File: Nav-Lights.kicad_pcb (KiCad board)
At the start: 4 copper layers, 40 x 10 mm, 29 parts, among them J1 Conn_01x02_Pin, U1 LMC555CMMX, U2 TPS7B8133QWDRVRQ1, U3 LT8374RUFM-WPBF

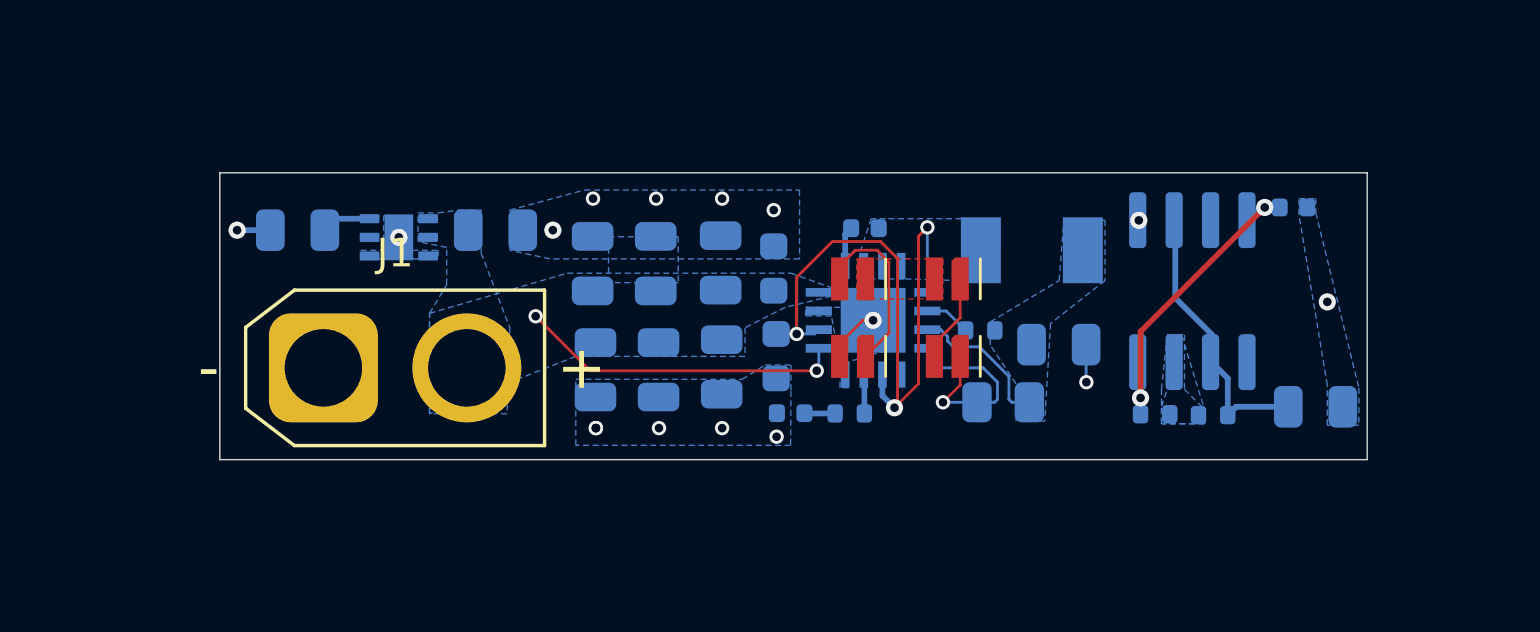
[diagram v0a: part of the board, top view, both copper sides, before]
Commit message: Adding in voltage divider for signal and layout and prod files
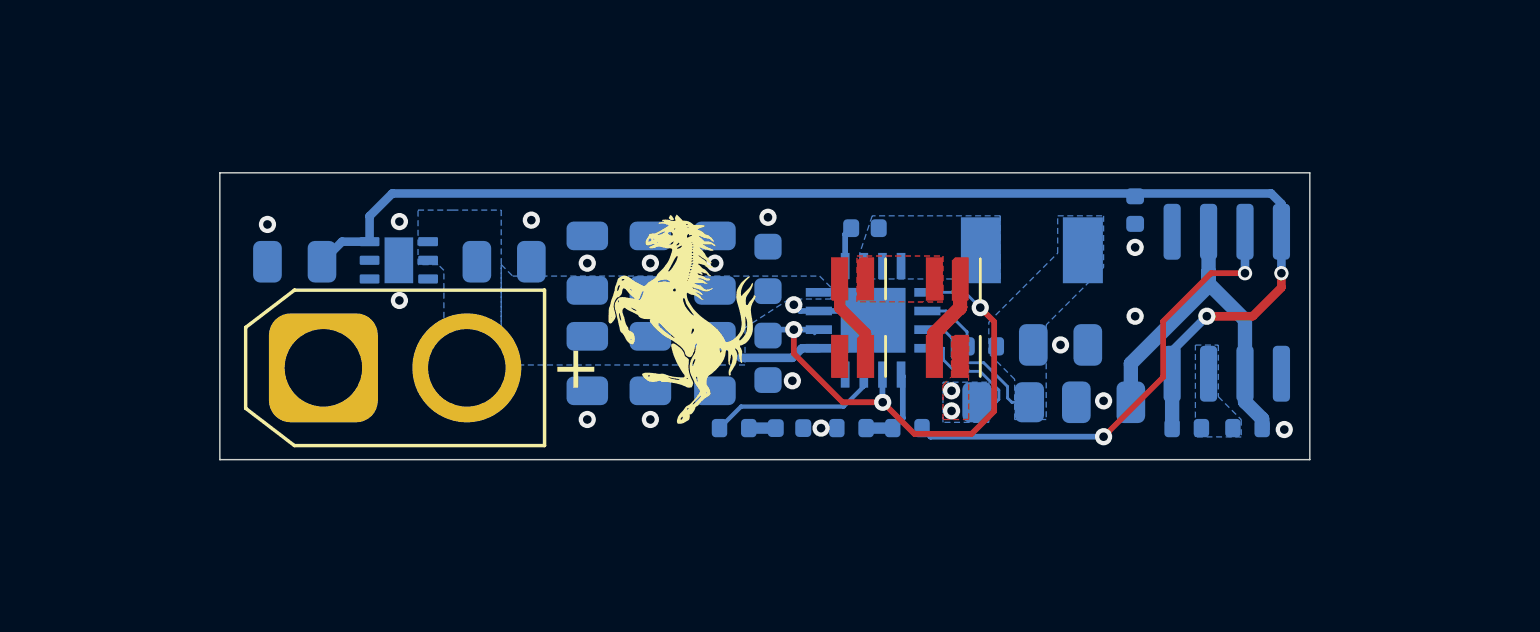
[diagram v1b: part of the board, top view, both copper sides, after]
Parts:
- added G***1: LOGO, LOGO, F.Cu at (143.4, 94.5)
- added R6: R_US, Resistor_SMD:R_0402_1005Metric, B.Cu at (151.3, 98.3)
- added R7: R_US, Resistor_SMD:R_0402_1005Metric, B.Cu at (149.3, 98.3)
- moved C3 7.39 mm to (158.1, 97.4), turned to 180 degrees
- moved C4 5.52 mm to (159.2, 90.7), turned to -90 degrees
- moved R4 4.06 mm to (145.2, 98.3), turned to 0 degrees
- moved R2 1.28 mm to (163.1, 98.3)
- moved U1 1.27 mm to (162.4, 93.9)
- moved R1 1.20 mm to (161.0, 98.3)
- moved C1 1.14 mm to (137.2, 92.5)
- moved C5 1.10 mm to (129.9, 92.5)
- moved U2 0.80 mm to (133.5, 92.5)
- moved R3 0.56 mm to (153.8, 95.5)
- moved C7 0.52 mm to (147.2, 98.3), turned to 0 degrees
- moved C14 0.36 mm to (140.1, 96.0)
- moved C16 0.36 mm to (142.3, 96.0)
- moved C8 0.29 mm to (146.4, 95.8)
- moved C15 0.26 mm to (144.6, 96.0)
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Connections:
- U3 pad 5: /Main/signal -> Net-(U3-CTRL)
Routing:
- net GND: track 69.6 -> 3.71 mm, vias 17 -> 18
- net +3V3: track 13.3 -> 45.3 mm
- net /Main/signal: track 0.00 -> 16.3 mm, vias 0 -> 2
- net /Main/VIN: track 11.4 -> 2.86 mm, vias 2 -> 0
- net /Main/INTVCC: track 23.8 -> 18.4 mm
- net Net-(U3-VC): track 1.36 -> 6.07 mm
- net /Main/THR: track 9.78 -> 13.3 mm
- net Net-(D3-K): track 6.19 -> 3.07 mm
- net /Main/ISN: track 7.52 -> 4.46 mm, vias 1 -> 2
- net Net-(U3-CTRL): track 0.00 -> 2.97 mm
- net Net-(U3-FB): track 1.61 -> 2.19 mm
- added copper zone on B.Cu, net /Main/ISN
- added copper zone on F.Cu, net /Main/ISN
- removed copper zone on B.Cu, net Net-(D2-K)
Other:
- board size 40 x 10 mm -> 38 x 10 mm
- board text added: "Nolan KM"
